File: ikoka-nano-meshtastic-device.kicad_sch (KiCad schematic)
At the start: 21 parts, among them J1 Qwiic_RA, J2 Solar, J3 Battery, J4 Battery, Q1 FDN302P, U1 Seeed Studio XIAO nRF52840, U2 E22-900M30S, U3 MT3608

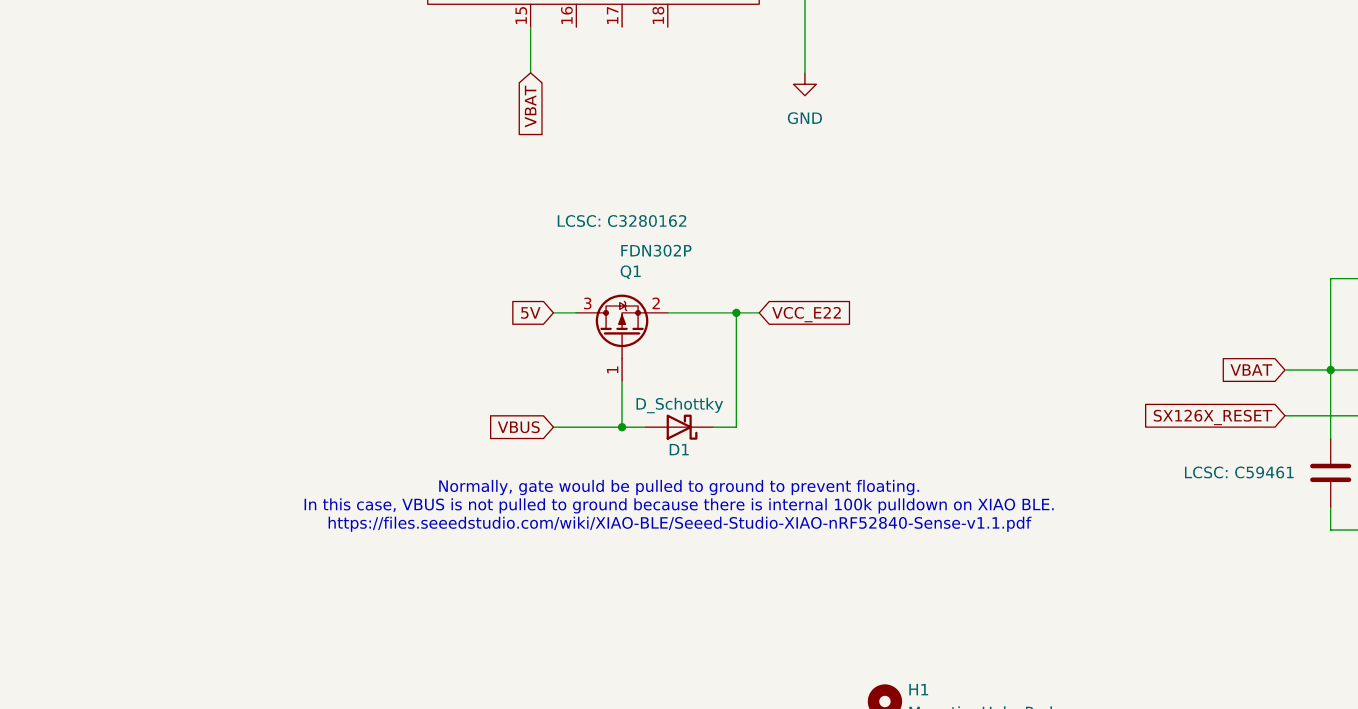
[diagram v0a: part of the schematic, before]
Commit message: Use AO3401A PMOS which is JLCPCB basic part
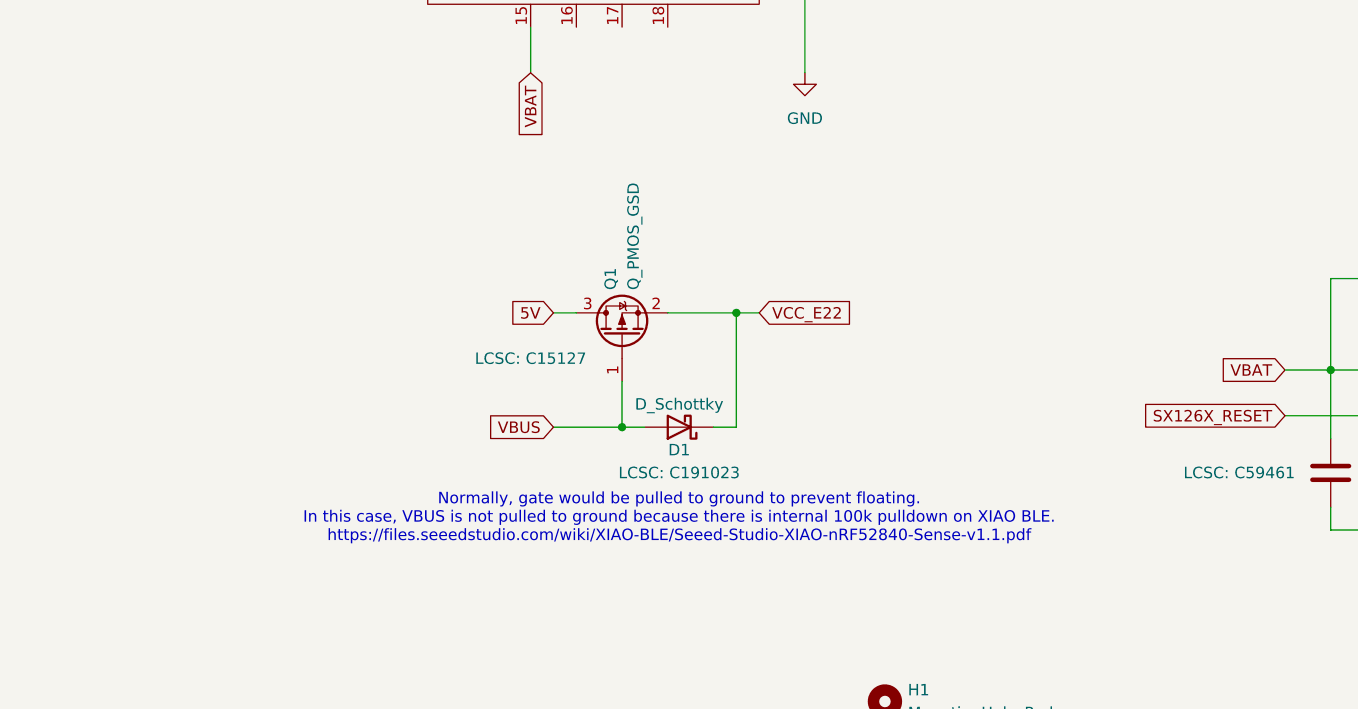
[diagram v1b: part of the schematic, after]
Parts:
- Q1: value FDN302P -> Q_PMOS_GSD; footprint Package_TO_SOT_SMD:SOT-23-3 -> Package_TO_SOT_SMD:SOT-23_Handsoldering; LCSC C3280162 -> C15127
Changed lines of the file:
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@@
 	(text "Normally, gate would be pulled to ground to prevent floating.\nIn this case, VBUS is not pulled to ground because there is internal 100k pulldown on XIAO BLE.\nhttps://files.seeedstudio.com/wiki/XIAO-BLE/Seeed-Studio-XIAO-nRF52840-Sense-v1.1.pdf"
 		(exclude_from_sim no)
-		(at 109.22 132.08 0)
+		(at 109.22 133.35 0)
 		(effects
 			(font
@@
 		)
 		(property "LCSC" "C191023"
-			(at 109.22 125.73 0)
-			(effects
-				(font
-					(size 1.27 1.27)
-				)
-				(hide yes)
+			(at 109.22 128.27 0)
+			(show_name yes)
+			(effects
+				(font
+					(size 1.27 1.27)
+				)
 			)
 		)
@@
 		(dnp no)
 		(property "Reference" "Q1"
-			(at 102.616 105.918 90)
-			(effects
-				(font
-					(size 1.27 1.27)
-				)
-				(justify right)
-			)
-		)
-		(property "Value" "FDN302P"
-			(at 102.616 103.632 90)
-			(effects
-				(font
-					(size 1.27 1.27)
-				)
-				(justify right)
-			)
-		)
-		(property "Footprint" "Package_TO_SOT_SMD:SOT-23-3"
+			(at 101.6 107.95 0)
+			(effects
+				(font
+					(size 1.27 1.27)
+				)
+				(justify left)
+			)
+		)
+		(property "Value" "Q_PMOS_GSD"
+			(at 104.14 107.95 0)
+			(effects
+				(font
+					(size 1.27 1.27)
+				)
+				(justify left)
+			)
+		)
+		(property "Footprint" "Package_TO_SOT_SMD:SOT-23_Handsoldering"
 			(at 100.33 107.95 0)
 			(effects
@@
 			)
 		)
-		(property "Datasheet" "https://www.lcsc.com/datasheet/lcsc_datasheet_2410010102_onsemi-FDN302P_C3280162.pdf"
+		(property "Datasheet" "~"
 			(at 102.87 113.03 0)
 			(effects
@@
 			)
 		)
-		(property "Description" "20V 2.4A 55mΩ@2.4A,4.5V 500mW 1.5V@250uA 1 Piece P-Channel SOT-23-3 MOSFETs ROHS"
+		(property "Description" "P-MOSFET transistor, gate/source/drain"
 			(at 102.87 113.03 0)
 			(effects
@@
 			)
 		)
-		(property "LCSC" "C3280162"
-			(at 102.87 100.33 90)
+		(property "LCSC" "C15127"
+			(at 92.71 115.57 90)
 			(show_name yes)
 			(effects
